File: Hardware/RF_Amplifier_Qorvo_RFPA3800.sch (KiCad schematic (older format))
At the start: 0 parts

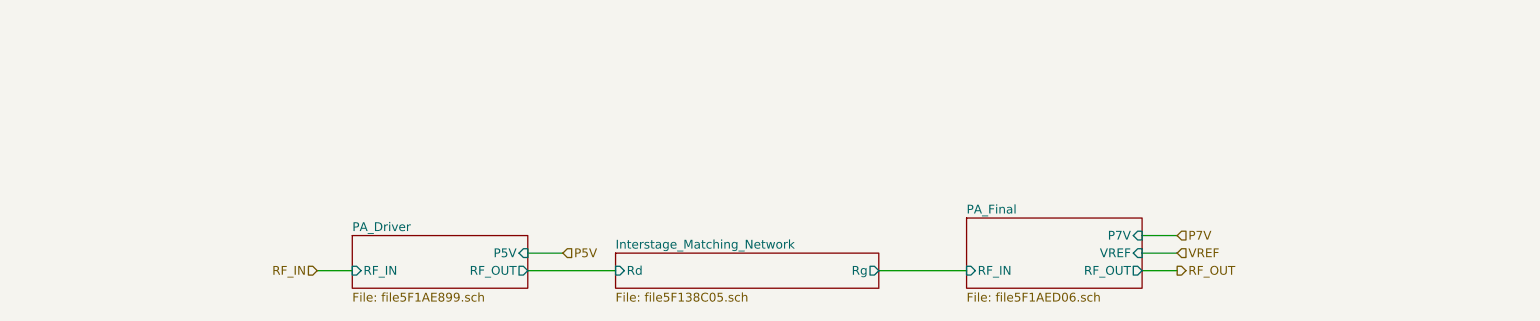
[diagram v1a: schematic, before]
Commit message: Major cleanup to both the schematic and directory structure. Stackup has changed accomodate to 0.65mm trace width. Chebyshev filter lived through the experience in the Qucs simulation; others not checked yet. I do want to re-visit the matching networks of all of the amplifiers as I have developed some good strategies to implement them.
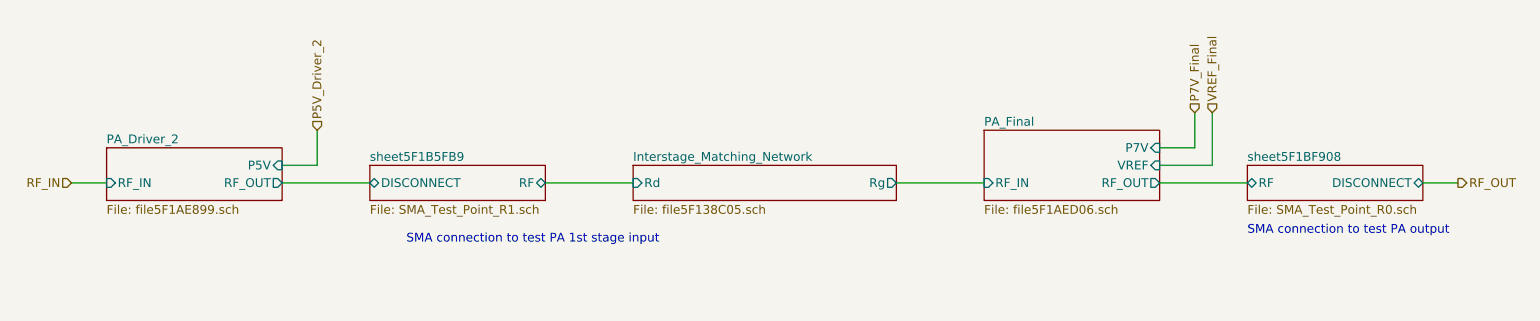
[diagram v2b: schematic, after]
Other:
- note added: "SMA connection to test PA 1st stage input"
- note added: "SMA connection to test PA output"
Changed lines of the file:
@@
 $Descr A4 11693 8268
 encoding utf-8
-Sheet 4 16
+Sheet 15 24
 Title ""
 Date ""
@@
 $EndDescr
 $Sheet
-S 4900 3800 1500 200
+S 5000 3300 1500 200
 U 5F138C06
 F0 "Interstage_Matching_Network" 50
 F1 "file5F138C05.sch" 50
-F2 "Rd" I L 4900 3900 50
-F3 "Rg" O R 6400 3900 50
+F2 "Rd" I L 5000 3400 50
+F3 "Rg" O R 6500 3400 50
 $EndSheet
 $Sheet
-S 3400 3700 1000 300
+S 2000 3200 1000 300
 U 5F1AE89A
-F0 "PA_Driver" 50
+F0 "PA_Driver_2" 50
 F1 "file5F1AE899.sch" 50
-F2 "RF_IN" I L 3400 3900 50
-F3 "P5V" I R 4400 3800 50
-F4 "RF_OUT" O R 4400 3900 50
+F2 "RF_IN" I L 2000 3400 50
+F3 "P5V" I R 3000 3300 50
+F4 "RF_OUT" O R 3000 3400 50
 $EndSheet
 $Sheet
-S 6900 3600 1000 400
+S 7000 3100 1000 400
 U 5F1AED07
 F0 "PA_Final" 50
 F1 "file5F1AED06.sch" 50
-F2 "RF_OUT" O R 7900 3900 50
-F3 "P7V" I R 7900 3700 50
-F4 "RF_IN" I L 6900 3900 50
-F5 "VREF" I R 7900 3800 50
+F2 "RF_OUT" O R 8000 3400 50
+F3 "P7V" I R 8000 3200 50
+F4 "RF_IN" I L 7000 3400 50
+F5 "VREF" I R 8000 3300 50
 $EndSheet
 Wire Wire Line
-	4400 3900 4900 3900
+	3000 3400 3500 3400
 Wire Wire Line
-	6400 3900 6900 3900
+	6500 3400 7000 3400
 Wire Wire Line
-	7900 3900 8100 3900
+	9500 3400 9700 3400
 Wire Wire Line
-	3400 3900 3200 3900
-Text HLabel 3200 3900 0    50   Input ~ 0
+	2000 3400 1800 3400
+Text HLabel 1800 3400 0    50   Input ~ 0
 RF_IN
-Text HLabel 8100 3900 2    50   Output ~ 0
+Text HLabel 9700 3400 2    50   Output ~ 0
 RF_OUT
+Text HLabel 8300 3000 1    50   Input ~ 0
+VREF_Final
 Wire Wire Line
-	7900 3800 8100 3800
-Text HLabel 8100 3800 2    50   Input ~ 0
-VREF
+	8000 3200 8200 3200
+Text HLabel 8200 3000 1    50   Input ~ 0
+P7V_Final
 Wire Wire Line
-	7900 3700 8100 3700
-Text HLabel 8100 3700 2    50   Input ~ 0
-P7V
+	3000 3300 3200 3300
+Text HLabel 3200 3100 1    50   Input ~ 0
+P5V_Driver_2
+$Sheet
+S 3500 3300 1000 200
+U 5F1B5FBD
+F0 "sheet5F1B5FB9" 50
+F1 "SMA_Test_Point_R1.sch" 50
+F2 "DISCONNECT" B L 3500 3400 50
+F3 "RF" B R 4500 3400 50
+$EndSheet
+Text Notes 5150 3750 2    50   ~ 0
+SMA connection to test PA 1st stage input
 Wire Wire Line
-	4400 3800 4600 3800
-Text HLabel 4600 3800 2    50   Input ~ 0
-P5V
+	3200 3300 3200 3100
+Text Notes 8500 3700 0    50   ~ 0
+SMA connection to test PA output
+$Sheet
+S 8500 3300 1000 200
+U 5F1BF90D
+F0 "sheet5F1BF908" 50
+F1 "SMA_Test_Point_R0.sch" 50
+F2 "DISCONNECT" B R 9500 3400 50
+F3 "RF" B L 8500 3400 50
+$EndSheet
+Wire Wire Line
+	8200 3000 8200 3200
+Wire Wire Line
+	8300 3000 8300 3300
+Wire Wire Line
+	8000 3300 8300 3300
+Wire Wire Line
+	8000 3400 8500 3400
+Wire Wire Line
+	4500 3400 5000 3400
 $EndSCHEMATC
